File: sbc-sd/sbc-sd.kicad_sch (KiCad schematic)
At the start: 21 parts, among them J1 SIO-Header, J2 RP2040-Zero-lhs, J3 RP2040-Zero-rhs, J4 RP2040-Zero-bottom, J5 104031-0811, U1 TXU0304, U2 LD39015M33R

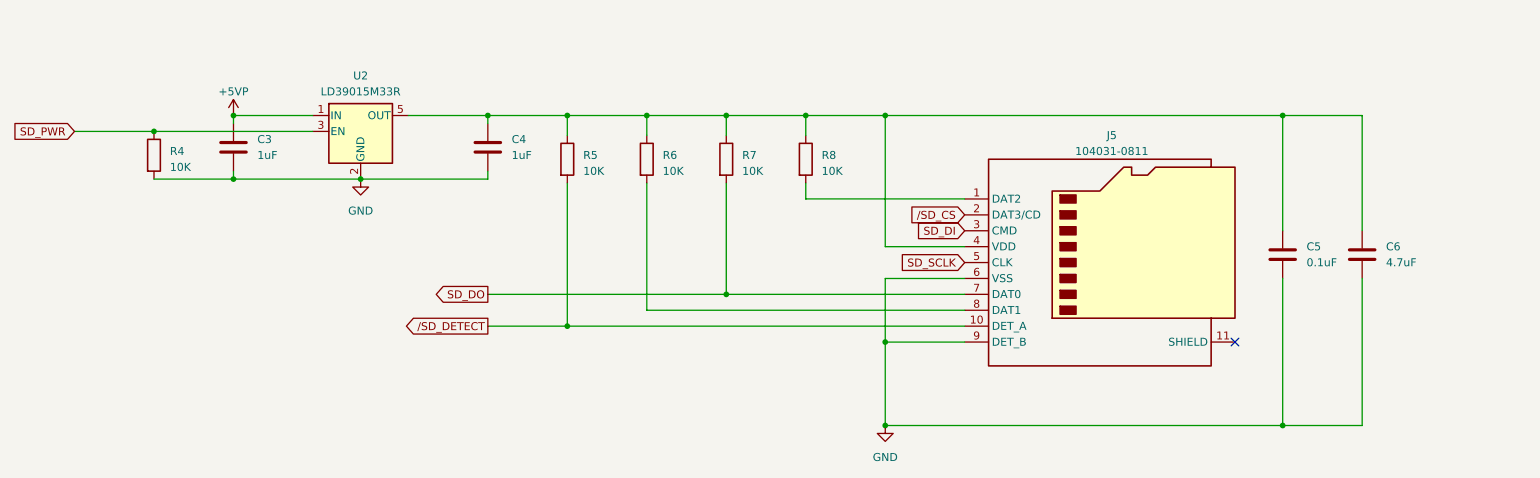
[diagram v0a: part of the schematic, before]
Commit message: SD card adapter v1.2
- Move SD card connector closer to the edge of the board
- Pullup SD detect signal to non-switched 5V
- Eliminate SD DO pullup
- Move LDO closer to SD
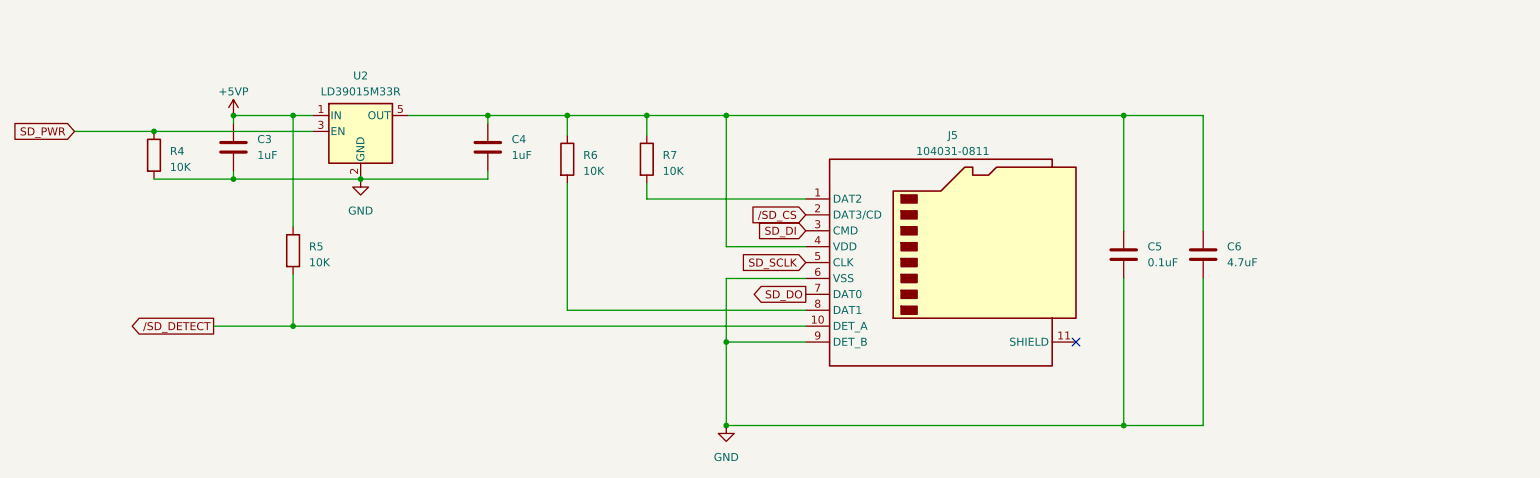
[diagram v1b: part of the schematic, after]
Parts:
- removed R7: 10K, Resistor_SMD:R_0805_2012Metric_Pad1.20x1.40mm_HandSolder, symbol Device:R
- renumbered R8 to R7
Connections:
- net +5VP: now also R5.1
- net at C4.1, C5.1, C6.1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: no longer R5.1
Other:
- moved on the sheet: C5, C6, J5, R5, R6, R7

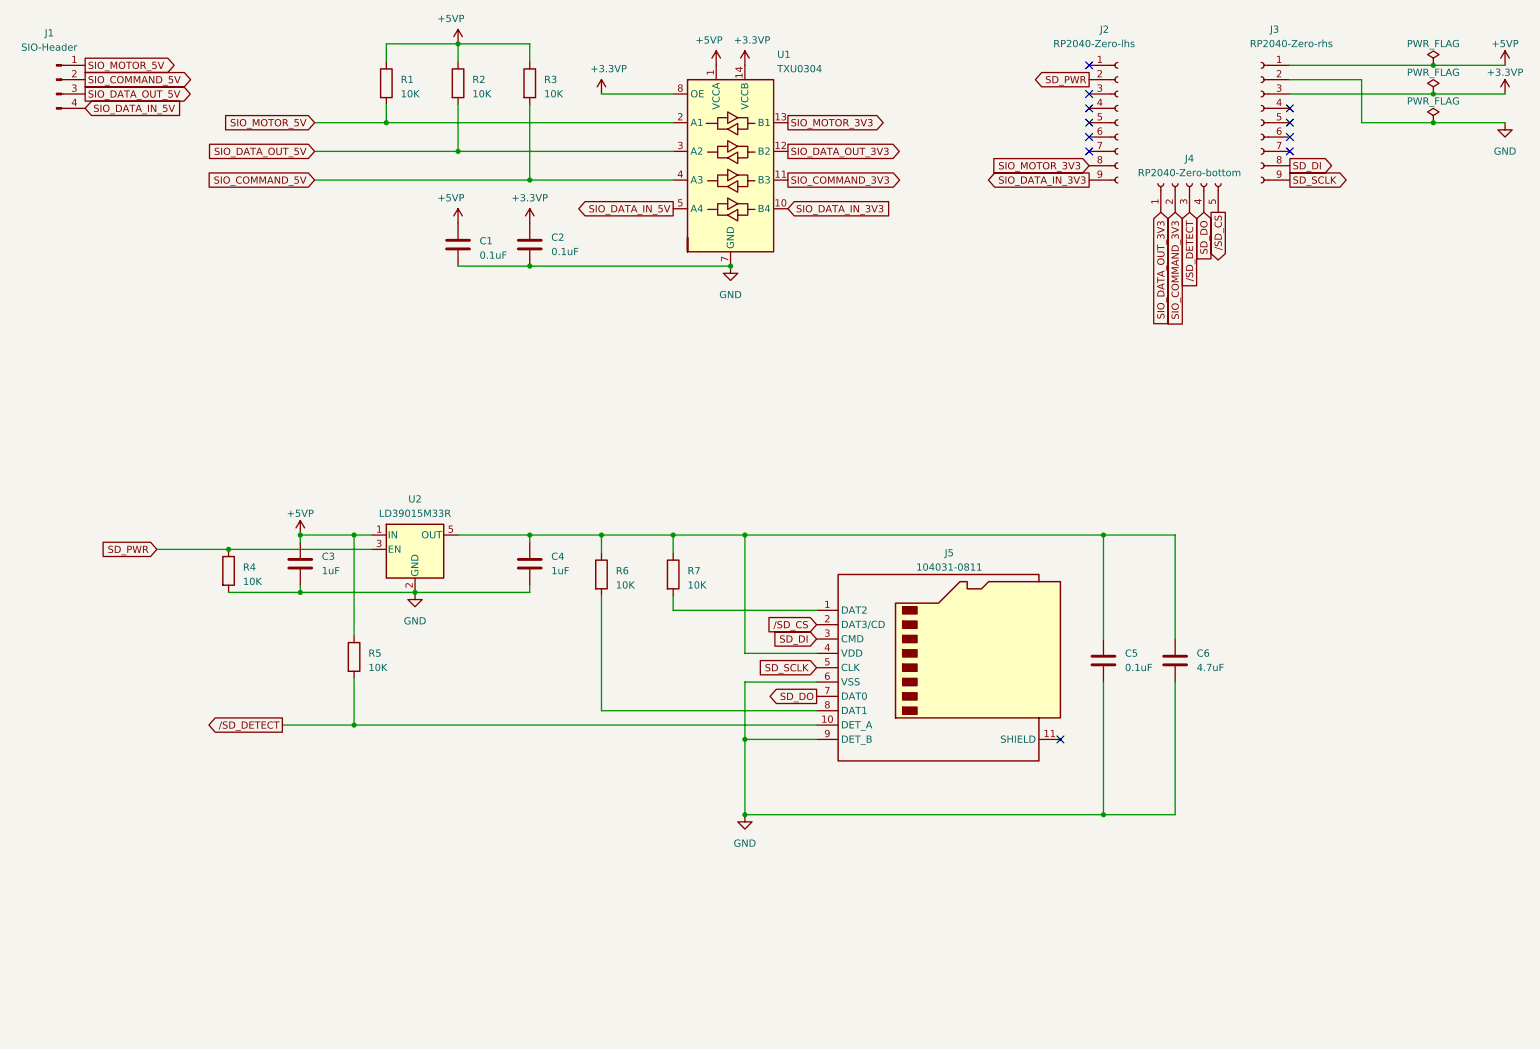
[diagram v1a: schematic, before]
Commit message: SBC v1.3
Motherboard updates:

  - KiCad 9 upgrade
  - USB-C power connector
  - Replace EOL resistor packs with discrete SMD resistors
  - Power/enable voltage translators from switched 5V
  - Fix motor signal pullup
  - Eliminate loop in phi2 traces
  - Thicker clock signal traces

SD card adapter updates:

  - KiCad 9 upgrade
  - Power/enable voltage translator from switched 5V and the eliminate unnecessary SIO pullups

Audio/Video adapter updates:

  - KiCad 9 upgrade
  - No functional changes, gerbers not regenerated, cleaned up bom
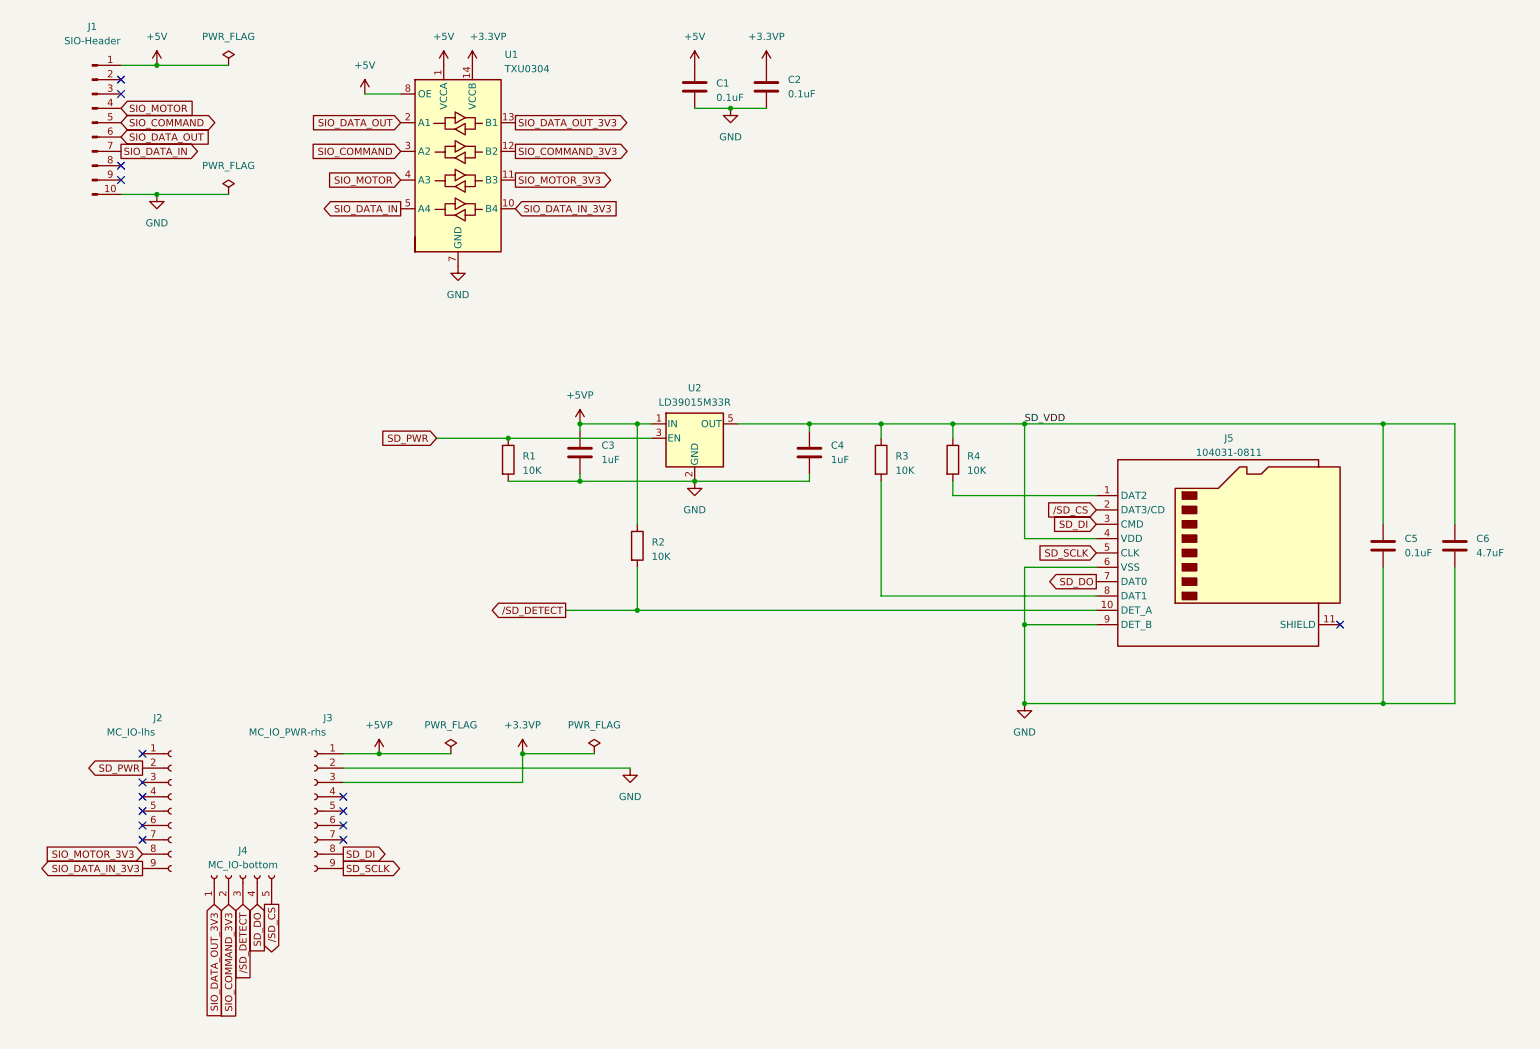
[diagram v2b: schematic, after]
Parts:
- removed J1: SIO-Header, Connector_PinHeader_2.54mm:PinHeader_1x04_P2.54mm_Vertical, symbol Connector:Conn_01x04_Pin
- removed R1, R2, R3: 10K, Resistor_SMD:R_0805_2012Metric_Pad1.20x1.40mm_HandSolder, symbol Device:R
- added J1: SIO-Header, Connector_PinHeader_2.54mm:PinHeader_1x10_P2.54mm_Vertical, symbol Connector:Conn_01x10_Pin
- J2: value RP2040-Zero-lhs -> MC_IO-lhs
- J3: value RP2040-Zero-rhs -> MC_IO_PWR-rhs
- J4: value RP2040-Zero-bottom -> MC_IO-bottom
- renumbered R4 to R1, R5 to R2, R6 to R3, R7 to R4
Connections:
- net +3.3VP: no longer U1.8 (OE)
- net +5VP: no longer C1.1, U1.1 (VCCA)
- net GND: now also J1.10 (Pin_10)
- net SIO_COMMAND_3V3: now also U1.12 (B2); no longer U1.11 (B3)
- net SIO_DATA_OUT_3V3: now also U1.13 (B1); no longer U1.12 (B2)
- net SIO_MOTOR_3V3: now also U1.11 (B3); no longer U1.13 (B1)
- net SD_VDD: now reaches C4.1, C5.1, C6.1, J5.4 (VDD), R3.1, R4.1, U2.5 (OUT)
- net SIO_COMMAND_5V renamed SIO_MOTOR
- net SIO_MOTOR: now also J1.4 (Pin_4)
- net SIO_DATA_IN_5V renamed SIO_DATA_IN
- net SIO_DATA_IN: now also J1.7 (Pin_7)
- net SIO_DATA_OUT_5V renamed SIO_COMMAND
- net SIO_COMMAND: now also J1.5 (Pin_5)
- net SIO_MOTOR_5V renamed SIO_DATA_OUT
- net SIO_DATA_OUT: now also J1.6 (Pin_6)
- new net +5V: C1.1, J1.1 (Pin_1), U1.1 (VCCA), U1.8 (OE)
- no-connect marks 11 -> 15
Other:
- moved on the sheet: C1, C2, C3, C4, C5, C6, J2, J3, J4, J5, R1, R2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
